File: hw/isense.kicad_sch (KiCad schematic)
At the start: 24 parts, among them J7 Conn_02x01, U11 TPS2553, U12 INA236, U13 INA236

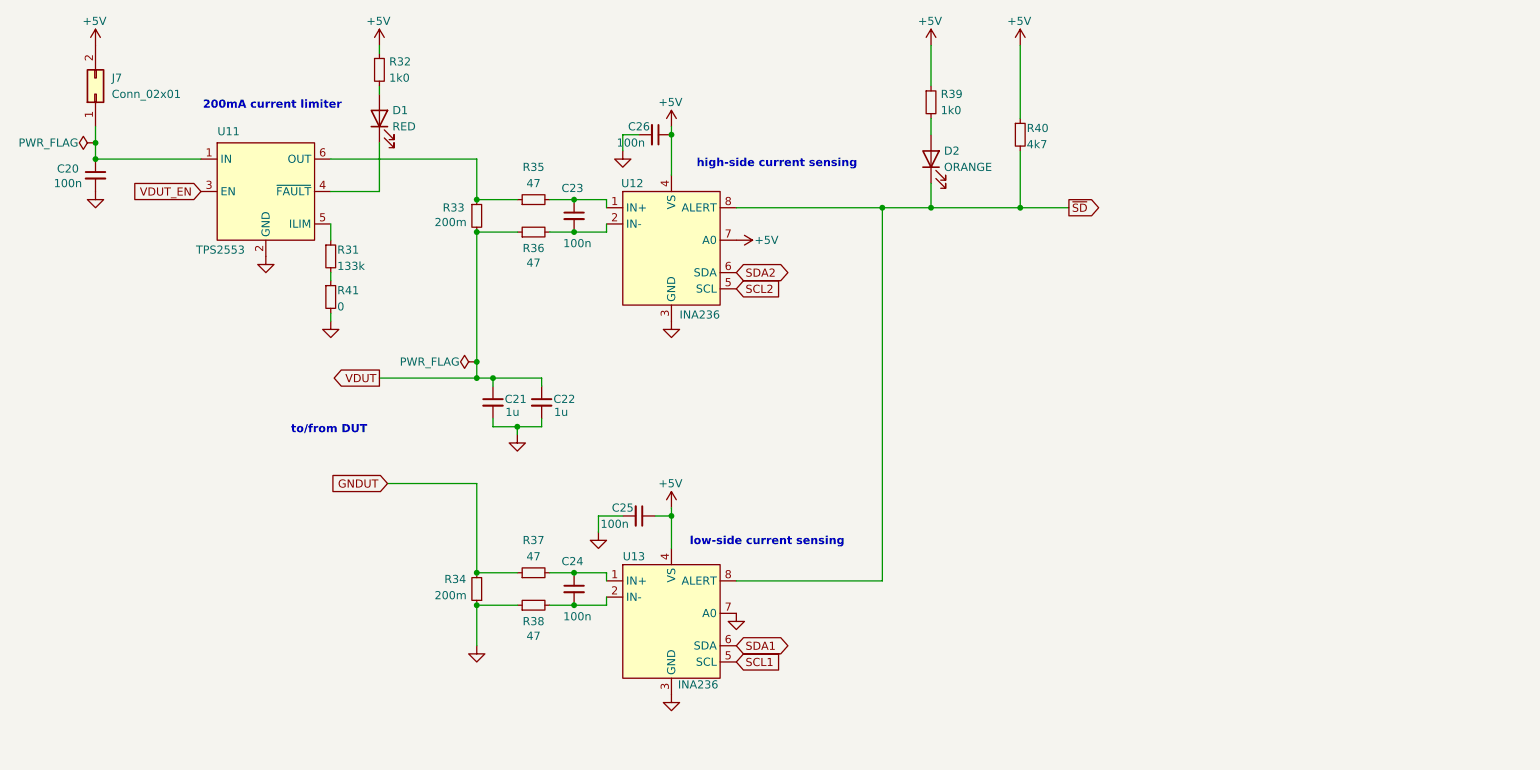
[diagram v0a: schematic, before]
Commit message: Specify INA236A, add note about INA236A/B variants
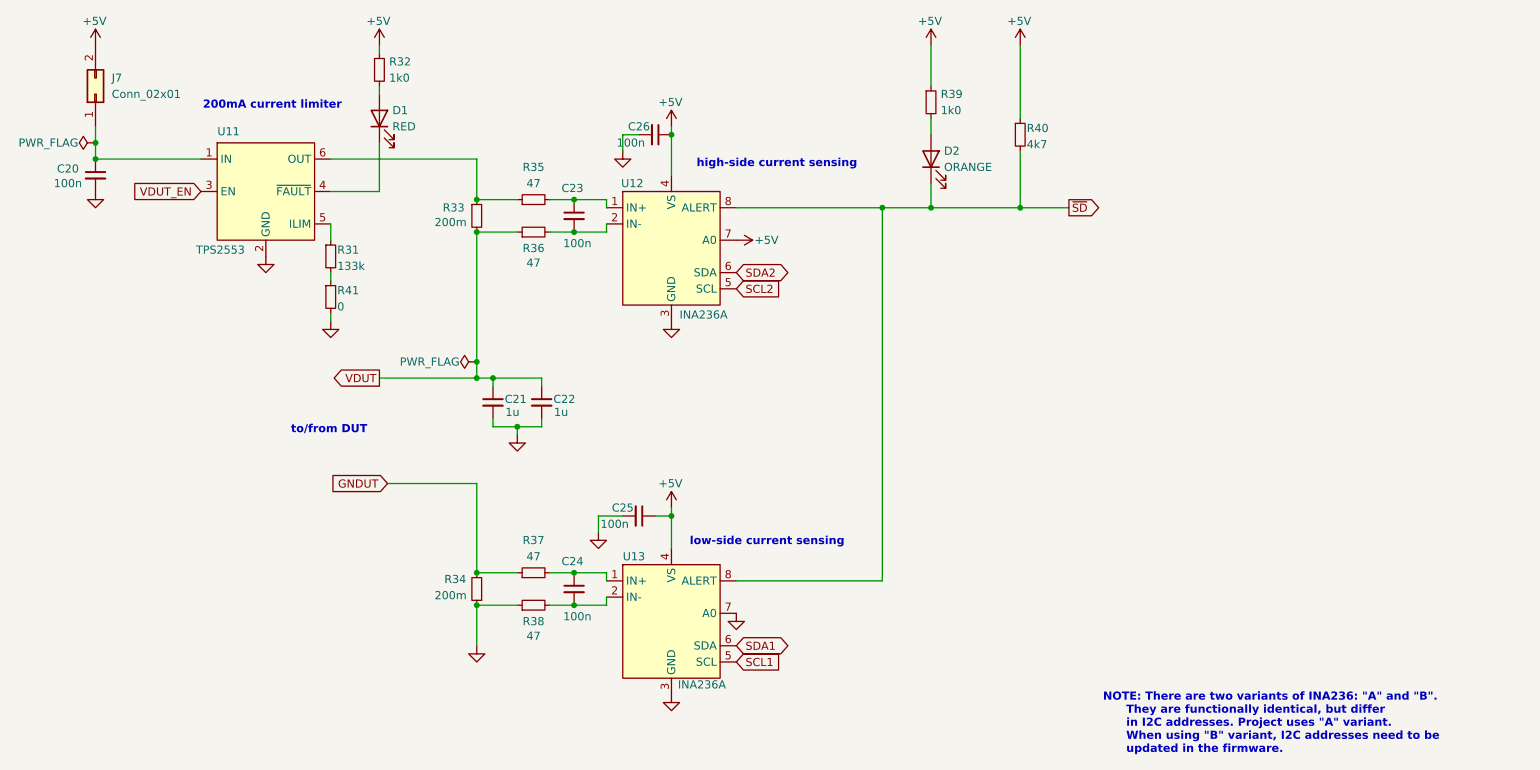
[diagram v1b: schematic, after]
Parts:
- U12, U13: value INA236 -> INA236A
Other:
- note added: "NOTE: There are two variants of INA236: "A" and "B". They are functionally identical, but differ in I2C addresses. Project uses "A" variant. When using "B" variant, I2C addresses need to be updated in the firmware."
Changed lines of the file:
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@@
+		)
+	)
+	(text "NOTE: There are two variants of INA236: \"A\" and \"B\".\n      They are functionally identical, but differ\n      in I2C addresses. Project uses \"A\" variant.\n      When using \"B\" variant, I2C addresses need to be\n      updated in the firmware."
+		(exclude_from_sim no)
+		(at 222.504 153.162 0)
+		(effects
+			(font
+				(size 1.27 1.27)
+				(thickness 0.254)
+				(bold yes)
+			)
+			(justify left)
 		)
 	)
@@
 			)
 		)
-		(property "Value" "INA236"
+		(property "Value" "INA236A"
 			(at 156.21 89.154 0)
 			(effects
@@
 			)
 		)
-		(property "Value" "INA236"
+		(property "Value" "INA236A"
 			(at 155.956 147.066 0)
 			(effects
